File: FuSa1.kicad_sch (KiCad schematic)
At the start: 0 parts

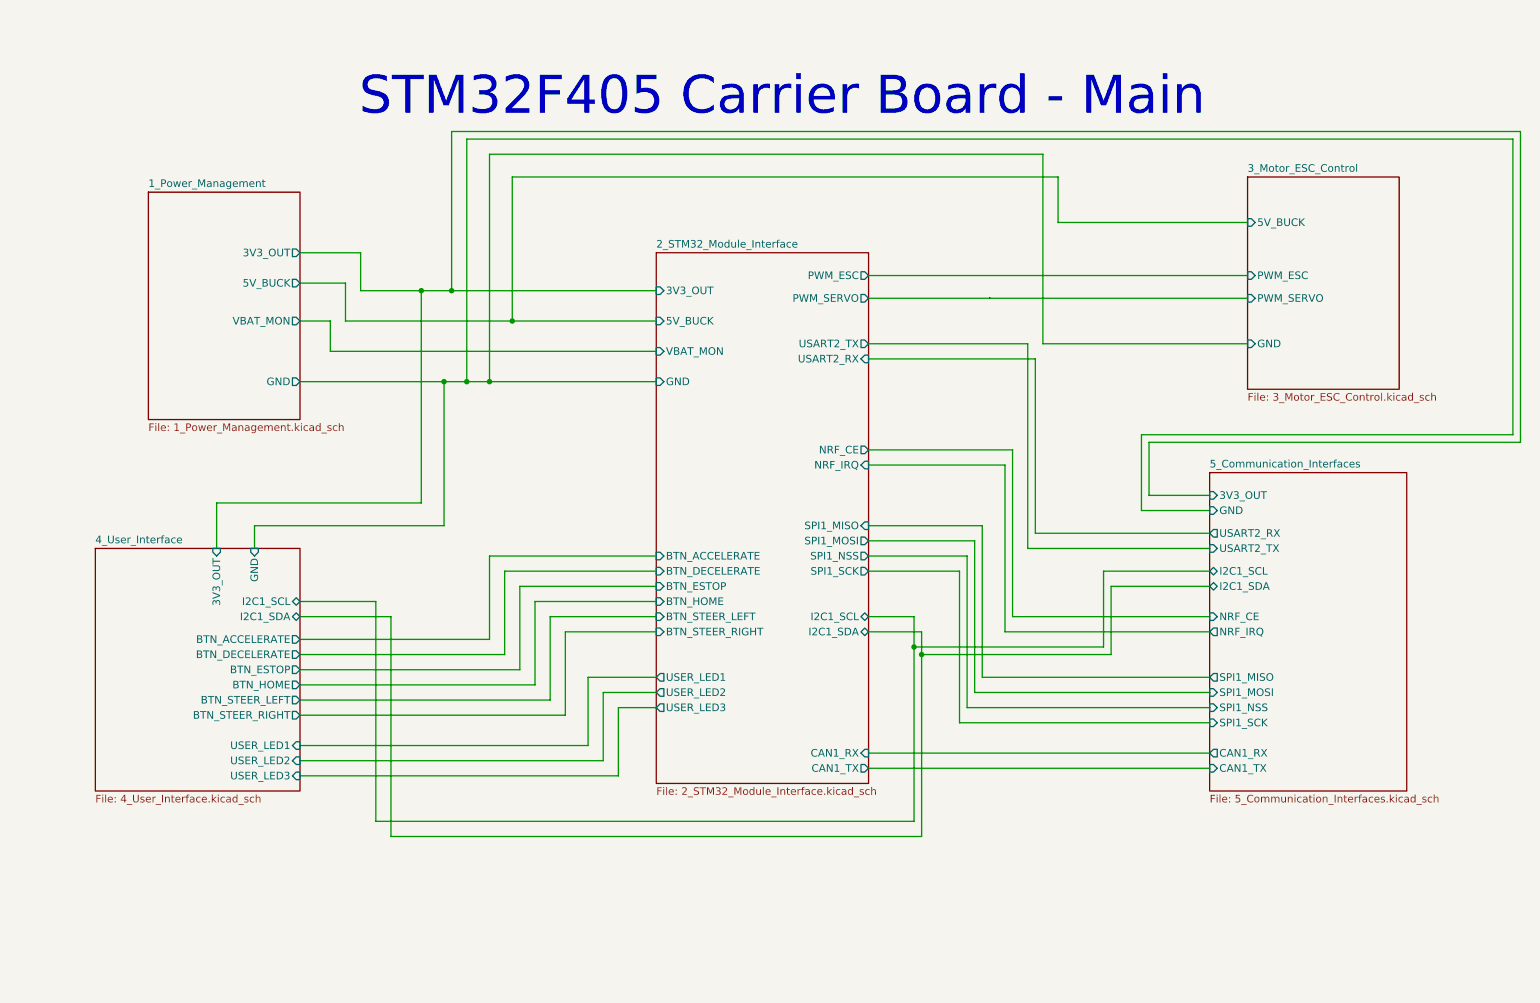
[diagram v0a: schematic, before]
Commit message: Cleaned up schematic. Added mounting holes.
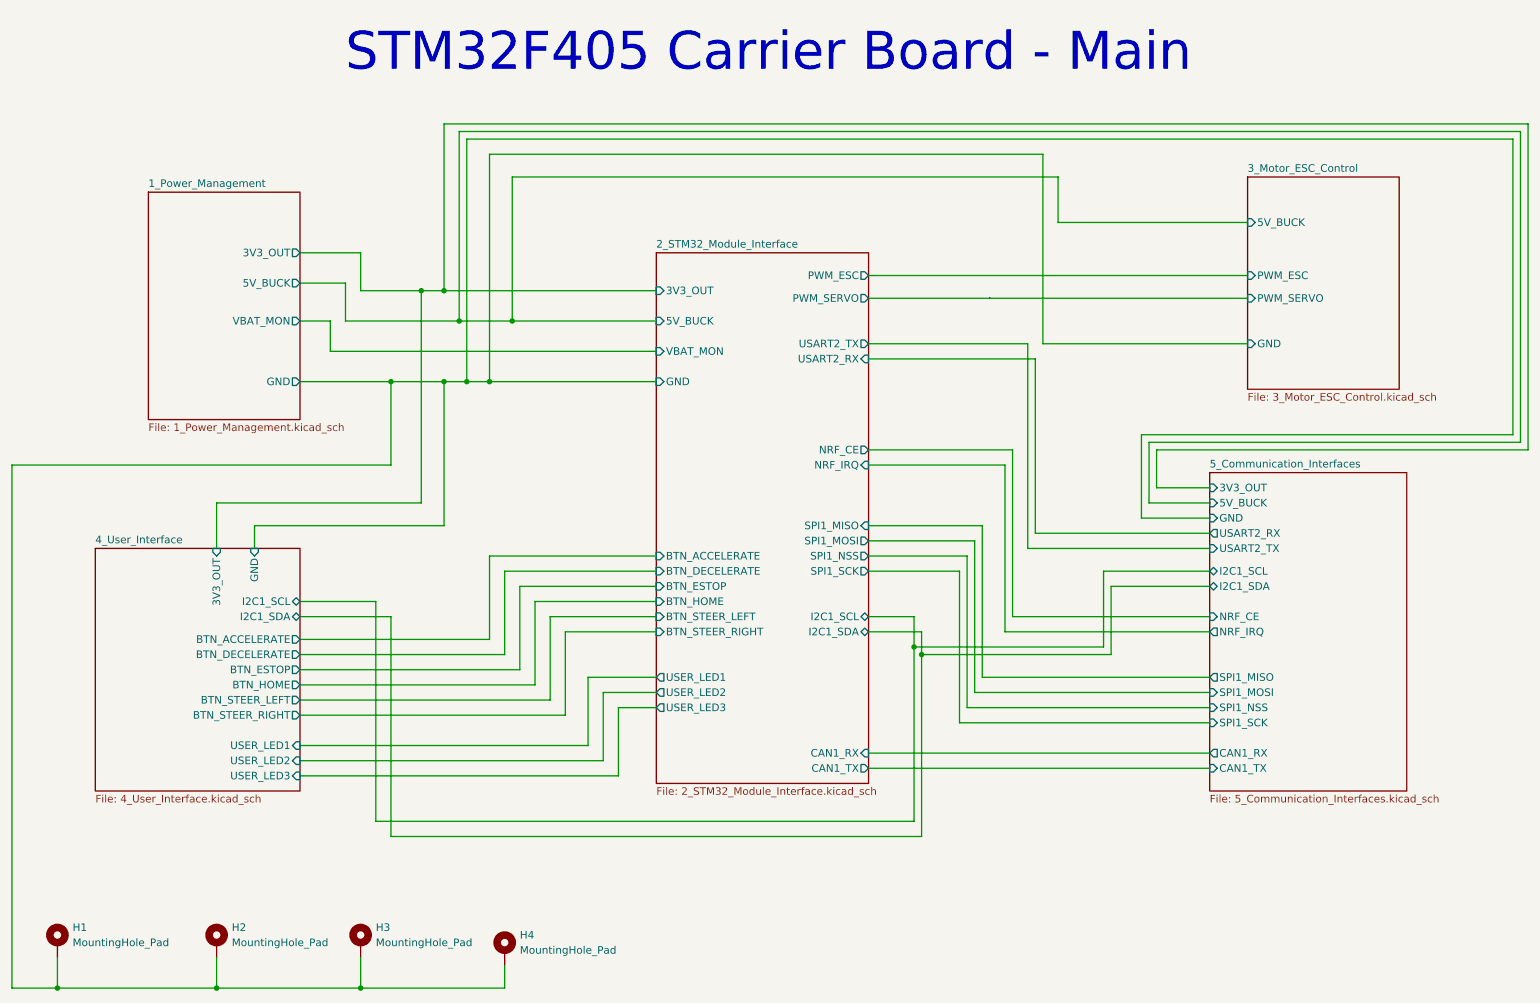
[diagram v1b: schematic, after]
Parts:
- added H1, H2, H3, H4: MountingHole_Pad, MountingHole:MountingHole_3.2mm_M3_Pad, symbol Mechanical:MountingHole_Pad
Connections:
- net 1_Power_Management/GND: now also H1.1, H2.1, H3.1, H4.1
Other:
- sheet 5_Communication_Interfaces ports: added 5V_BUCK; removed none
